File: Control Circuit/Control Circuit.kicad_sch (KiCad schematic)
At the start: 5 parts, among them U1 Adafruit DPS310, U3 Adafruit BNO085, U4 TPS61087

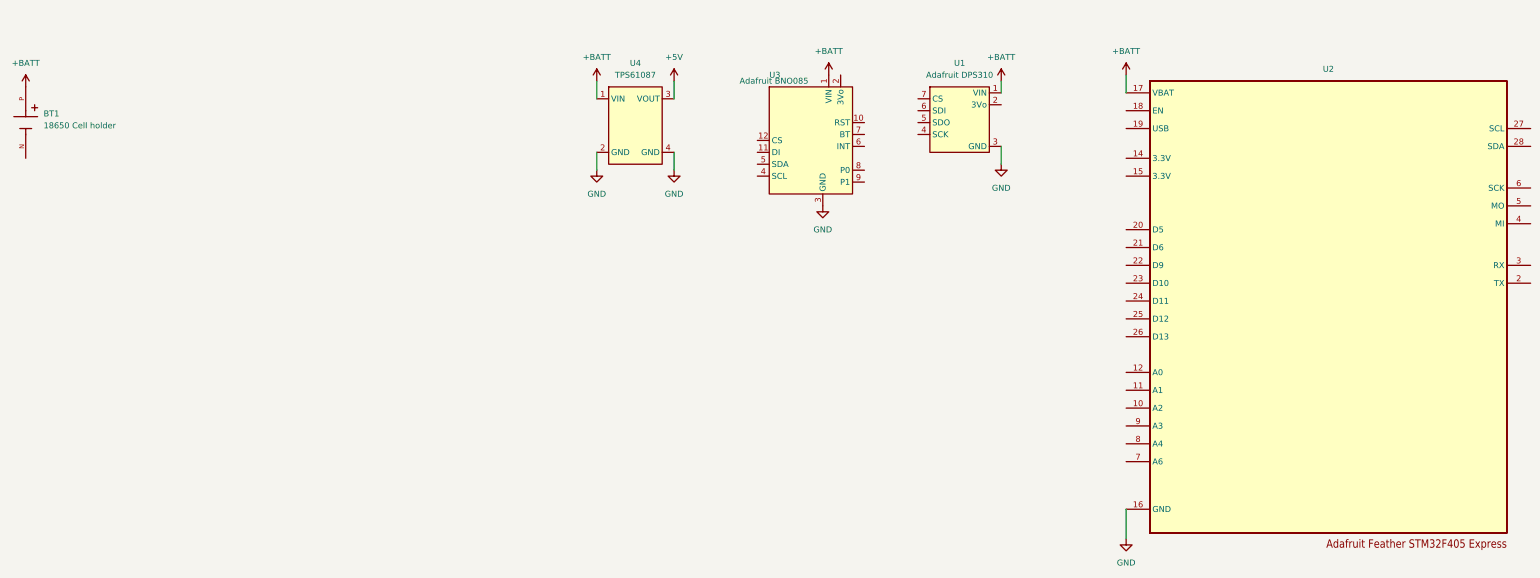
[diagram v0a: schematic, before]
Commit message: switching from development board to on board chip
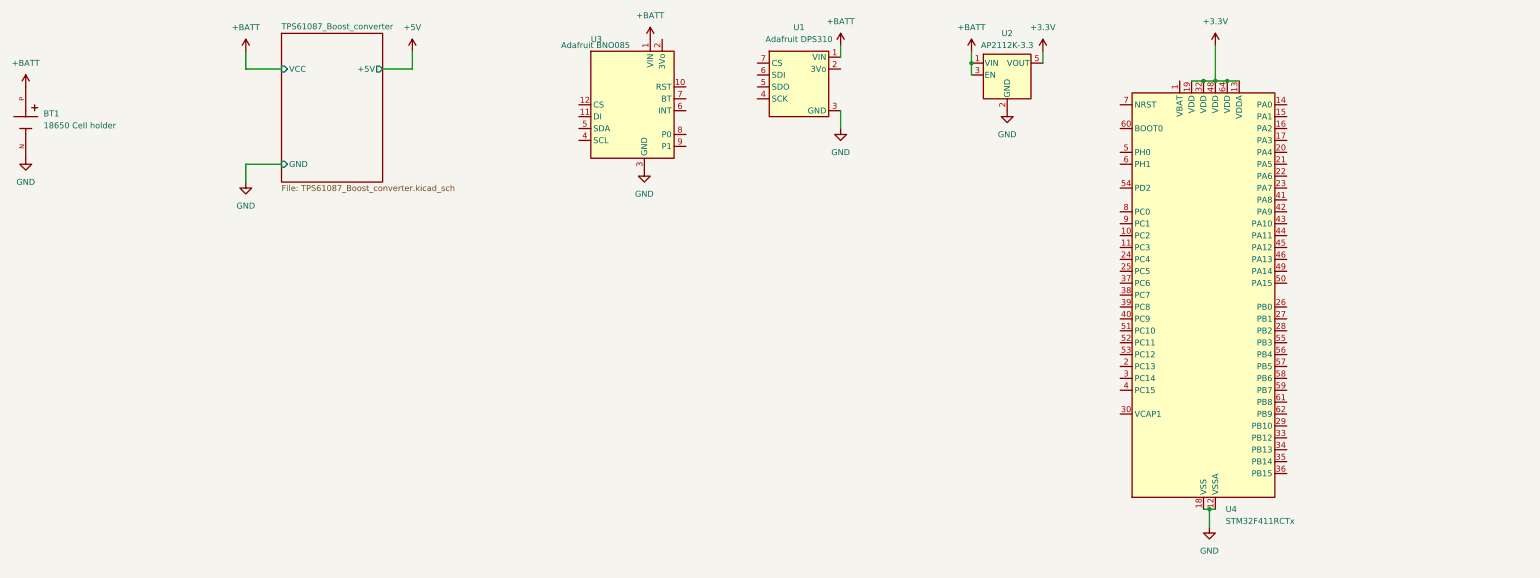
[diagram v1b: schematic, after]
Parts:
- removed U2: ~, STM32F405:Adafruit Feather STM32F405 Express, symbol Adafruit STM32F405:Adafruit_express_STM32F405
- removed U4: TPS61087, Boost Converter:TPS61087 Breakout, symbol Boost Converter:Boost_Converter
- added U2: AP2112K-3.3, Package_TO_SOT_SMD:SOT-23-5, symbol Regulator_Linear:AP2112K-3.3
- added U4: STM32F411RCTx, Package_QFP:LQFP-64_10x10mm_P0.5mm, symbol MCU_ST_STM32F4:STM32F411RCTx
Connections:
- net +BATT: now also U2.1 (VIN), U2.3 (EN)
- net GND: now also BT1.N, U2.2 (GND), U4.12 (VSSA), U4.18 (VSS), U4.31 (VSS), U4.47 (VSS), U4.63 (VSS)
- new net +3.3V: U2.5 (VOUT), U4.13 (VDDA), U4.19 (VDD), U4.32 (VDD), U4.48 (VDD), U4.64 (VDD)
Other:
- added sheet TPS61087_Boost_converter (TPS61087_Boost_converter.kicad_sch)
- moved on the sheet: U1, U3

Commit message: dropped gitignore files
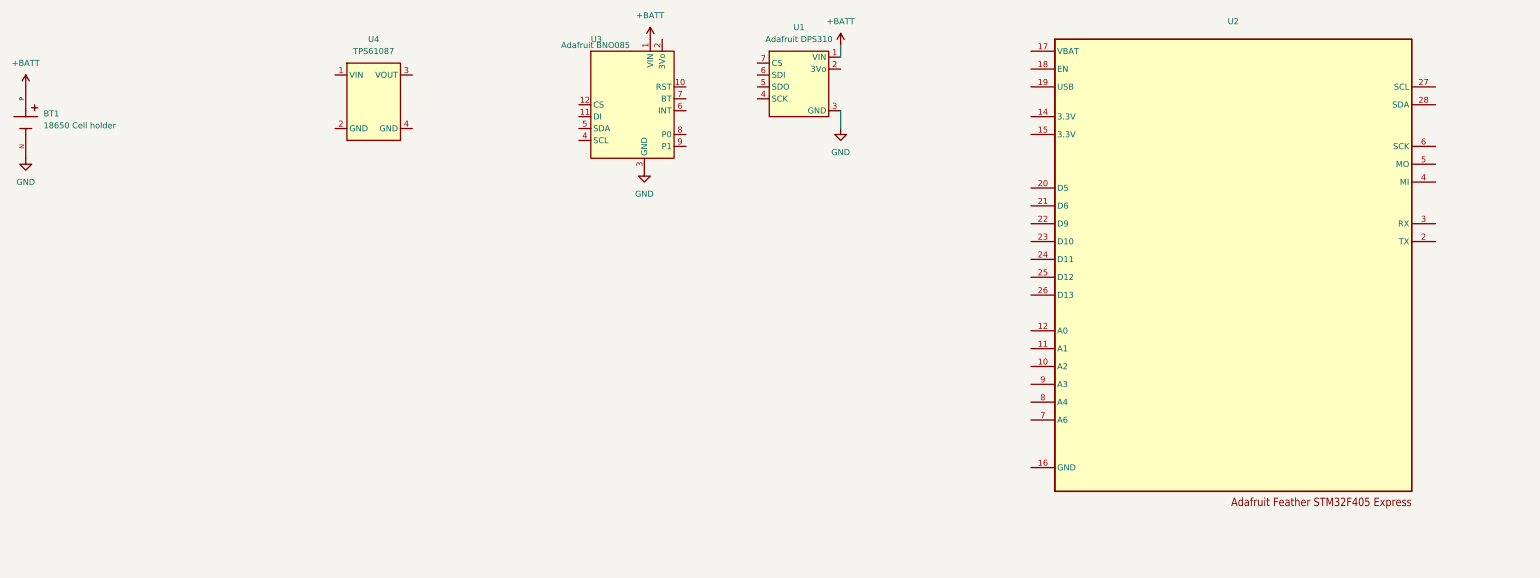
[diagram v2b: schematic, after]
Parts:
- removed U2: AP2112K-3.3, Package_TO_SOT_SMD:SOT-23-5, symbol Regulator_Linear:AP2112K-3.3
- removed U4: STM32F411RCTx, Package_QFP:LQFP-64_10x10mm_P0.5mm, symbol MCU_ST_STM32F4:STM32F411RCTx
- added U2: ~, STM32F405:Adafruit Feather STM32F405 Express, symbol Adafruit STM32F405:Adafruit_express_STM32F405
- added U4: TPS61087, Boost Converter:TPS61087 Breakout, symbol Boost Converter:Boost_Converter
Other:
- removed sheet TPS61087_Boost_converter
